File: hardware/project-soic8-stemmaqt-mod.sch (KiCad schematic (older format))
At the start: 2 parts, among them J1 SM04B-SRSS-TB(LF)(SN), U1 24LC00

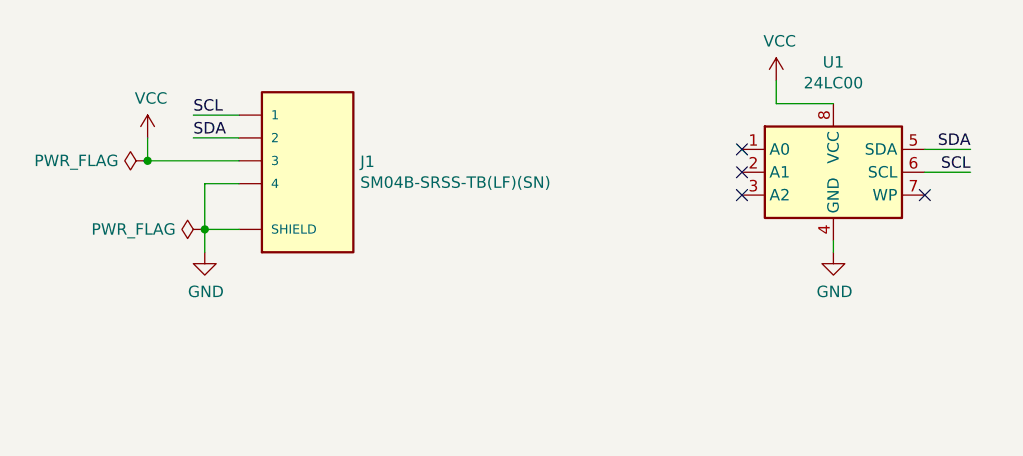
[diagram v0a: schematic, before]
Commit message: Add cable type note
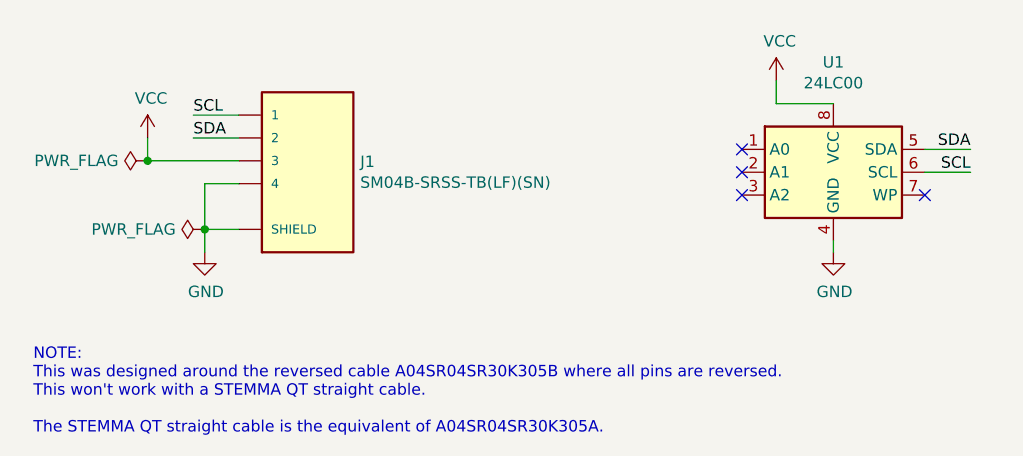
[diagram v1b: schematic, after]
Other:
- note added: "NOTE:\nThis was designed around the reversed cable A04SR04SR30K305B where all pins are reversed.\nThis won't work with a STEMMA QT straight cable.\n\nThe STEMMA QT straight cable is the equivalent of A04SR04SR30K305A."
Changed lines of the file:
@@
 Text Label 4750 1250 2    50   ~ 0
 SDA
+Text Notes 650  2500 0    50   ~ 0
+NOTE:\nThis was designed around the reversed cable A04SR04SR30K305B where all pins are reversed.\nThis won't work with a STEMMA QT straight cable.\n\nThe STEMMA QT straight cable is the equivalent of A04SR04SR30K305A.
 $EndSCHEMATC

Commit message: Match Stemma QT pinout
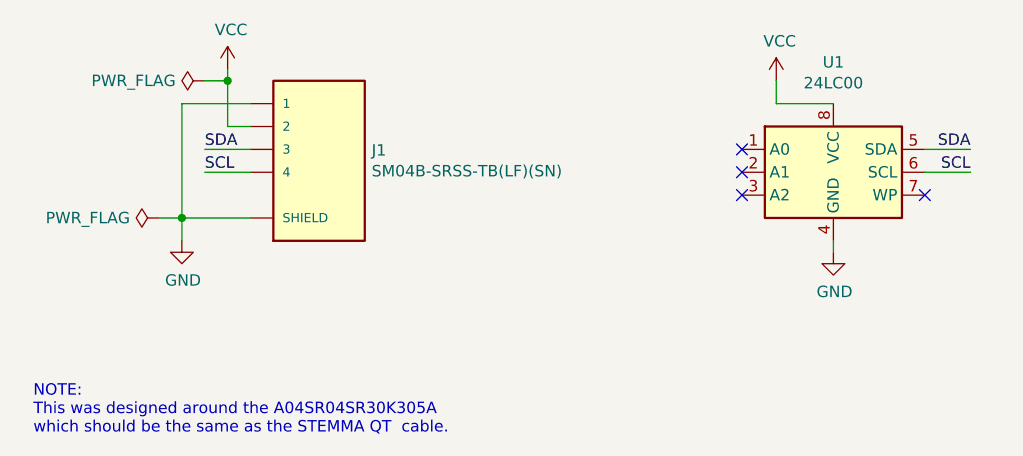
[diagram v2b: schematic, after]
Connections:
- net GND: now also J1.1; no longer J1.4
- net SCL: now also J1.4; no longer J1.1
- net SDA: now also J1.3; no longer J1.2
- net VCC: now also J1.2; no longer J1.3
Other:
- note added: "NOTE:\nThis was designed around the A04SR04SR30K305A\nwhich should be the same as the STEMMA QT cable."
- note removed: "NOTE:\nThis was designed around the reversed cable A04SR04SR30K305B where all pins are reversed.\nThis won't work with a STEMMA QT straight cable.\n\nThe STEMMA QT straight cable is the equivalent of A04SR04SR30K305A."
- moved on the sheet: J1
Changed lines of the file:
@@
 L SM04B-SRSS-TB_LF__SN_:SM04B-SRSS-TB(LF)(SN) J1
 U 1 1 6096D0A7
-P 1850 1300
-F 0 "J1" H 2080 1296 50  0000 L CNN
-F 1 "SM04B-SRSS-TB(LF)(SN)" H 2080 1205 50  0000 L CNN
-F 2 "SM04B-SRSS-TB(LF)(SN):JST_SM04B-SRSS-TB(LF)(SN)" H 1850 1300 50  0001 L BNN
-F 3 "" H 1850 1300 50  0001 L BNN
-F 4 "Manufacturer recommendations" H 1850 1300 50  0001 L BNN "STANDARD"
-F 5 "JST" H 1850 1300 50  0001 L BNN "MANUFACTURER"
-	1    1850 1300
+P 1900 1250
+F 0 "J1" H 2130 1246 50  0000 L CNN
+F 1 "SM04B-SRSS-TB(LF)(SN)" H 2130 1155 50  0000 L CNN
+F 2 "SM04B-SRSS-TB(LF)(SN):JST_SM04B-SRSS-TB(LF)(SN)" H 1900 1250 50  0001 L BNN
+F 3 "" H 1900 1250 50  0001 L BNN
+F 4 "Manufacturer recommendations" H 1900 1250 50  0001 L BNN "STANDARD"
+F 5 "JST" H 1900 1250 50  0001 L BNN "MANUFACTURER"
+	1    1900 1250
 	1    0    0    -1
 $EndComp
 Wire Wire Line
-	1350 1100 1550 1100
-Text Label 1350 1100 0    50   ~ 0
+	1400 1350 1600 1350
+Text Label 1400 1350 0    50   ~ 0
 SCL
 Wire Wire Line
-	1350 1200 1550 1200
-Text Label 1350 1200 0    50   ~ 0
+	1400 1250 1600 1250
+Text Label 1400 1250 0    50   ~ 0
 SDA
 $Comp
 L power:GND #PWR02
 U 1 1 60970746
-P 1400 1700
-F 0 "#PWR02" H 1400 1450 50  0001 C CNN
-F 1 "GND" H 1405 1527 50  0000 C CNN
-F 2 "" H 1400 1700 50  0001 C CNN
-F 3 "" H 1400 1700 50  0001 C CNN
-	1    1400 1700
+P 1300 1650
+F 0 "#PWR02" H 1300 1400 50  0001 C CNN
+F 1 "GND" H 1305 1477 50  0000 C CNN
+F 2 "" H 1300 1650 50  0001 C CNN
+F 3 "" H 1300 1650 50  0001 C CNN
+	1    1300 1650
+	1    0    0    -1
+$EndComp
+$Comp
+L power:VCC #PWR01
+U 1 1 609711EA
+P 1500 900
+F 0 "#PWR01" H 1500 750 50  0001 C CNN
+F 1 "VCC" H 1515 1073 50  0000 C CNN
+F 2 "" H 1500 900 50  0001 C CNN
+F 3 "" H 1500 900 50  0001 C CNN
+	1    1500 900
 	1    0    0    -1
 $EndComp
 Wire Wire Line
-	1400 1700 1400 1600
-Wire Wire Line
-	1400 1600 1550 1600
-Wire Wire Line
-	1400 1600 1400 1400
-Wire Wire Line
-	1400 1400 1550 1400
-Connection ~ 1400 1600
-$Comp
-L power:VCC #PWR01
-U 1 1 609711EA
-P 1150 1200
-F 0 "#PWR01" H 1150 1050 50  0001 C CNN
-F 1 "VCC" H 1165 1373 50  0000 C CNN
-F 2 "" H 1150 1200 50  0001 C CNN
-F 3 "" H 1150 1200 50  0001 C CNN
-	1    1150 1200
-	1    0    0    -1
-$EndComp
-Wire Wire Line
-	1150 1300 1150 1200
-Wire Wire Line
-	1150 1300 1550 1300
+	1500 1150 1500 950
 $Comp
 L power:VCC #PWR03
@@
 L power:PWR_FLAG #FLG01
 U 1 1 6097872C
-P 1150 1300
-F 0 "#FLG01" H 1150 1375 50  0001 C CNN
-F 1 "PWR_FLAG" V 1150 1427 50  0000 L CNN
-F 2 "" H 1150 1300 50  0001 C CNN
-F 3 "~" H 1150 1300 50  0001 C CNN
-	1    1150 1300
+P 1400 950
+F 0 "#FLG01" H 1400 1025 50  0001 C CNN
+F 1 "PWR_FLAG" V 1400 1077 50  0000 L CNN
+F 2 "" H 1400 950 50  0001 C CNN
+F 3 "~" H 1400 950 50  0001 C CNN
+	1    1400 950
 	0    -1   -1   0
 $EndComp
-Connection ~ 1150 1300
 $Comp
 L power:PWR_FLAG #FLG02
 U 1 1 609794A0
-P 1400 1600
-F 0 "#FLG02" H 1400 1675 50  0001 C CNN
-F 1 "PWR_FLAG" V 1400 1727 50  0000 L CNN
-F 2 "" H 1400 1600 50  0001 C CNN
-F 3 "~" H 1400 1600 50  0001 C CNN
-	1    1400 1600
+P 1200 1550
+F 0 "#FLG02" H 1200 1625 50  0001 C CNN
+F 1 "PWR_FLAG" V 1200 1677 50  0000 L CNN
+F 2 "" H 1200 1550 50  0001 C CNN
+F 3 "~" H 1200 1550 50  0001 C CNN
+	1    1200 1550
 	0    -1   -1   0
 $EndComp
@@
 SDA
 Text Notes 650  2500 0    50   ~ 0
-NOTE:\nThis was designed around the reversed cable A04SR04SR30K305B where all pins are reversed.\nThis won't work with a STEMMA QT straight cable.\n\nThe STEMMA QT straight cable is the equivalent of A04SR04SR30K305A.
+NOTE:\nThis was designed around the A04SR04SR30K305A\nwhich should be the same as the STEMMA QT  cable.
+Wire Wire Line
+	1300 1550 1600 1550
+Wire Wire Line
+	1300 1650 1300 1550
+Connection ~ 1300 1550
+Wire Wire Line
+	1200 1550 1300 1550
+Wire Wire Line
+	1400 950  1500 950
+Wire Wire Line
+	1500 1150 1600 1150
+Connection ~ 1500 950
+Wire Wire Line
+	1500 950  1500 900
+Wire Wire Line
+	1600 1050 1300 1050
+Wire Wire Line
+	1300 1050 1300 1550
 $EndSCHEMATC
